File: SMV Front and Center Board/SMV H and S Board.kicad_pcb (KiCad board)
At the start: 2 copper layers, 65 parts, among them J1 430450200, J10 Molex Micro-Fit 4 Pin, J2 430450200, J4 22035035, J5 22035035, J6 22035035, J7 22035035, J8 430450200, Q1 PSMN1R8-40YLC_115, Q2 PSMN1R8-40YLC_115, U1 UA78M05QDCYRG4Q1, U2 MCP6286T-E/OT, U3 PADS131M04QPWRQ1, U4 MCP6286T-E/OT

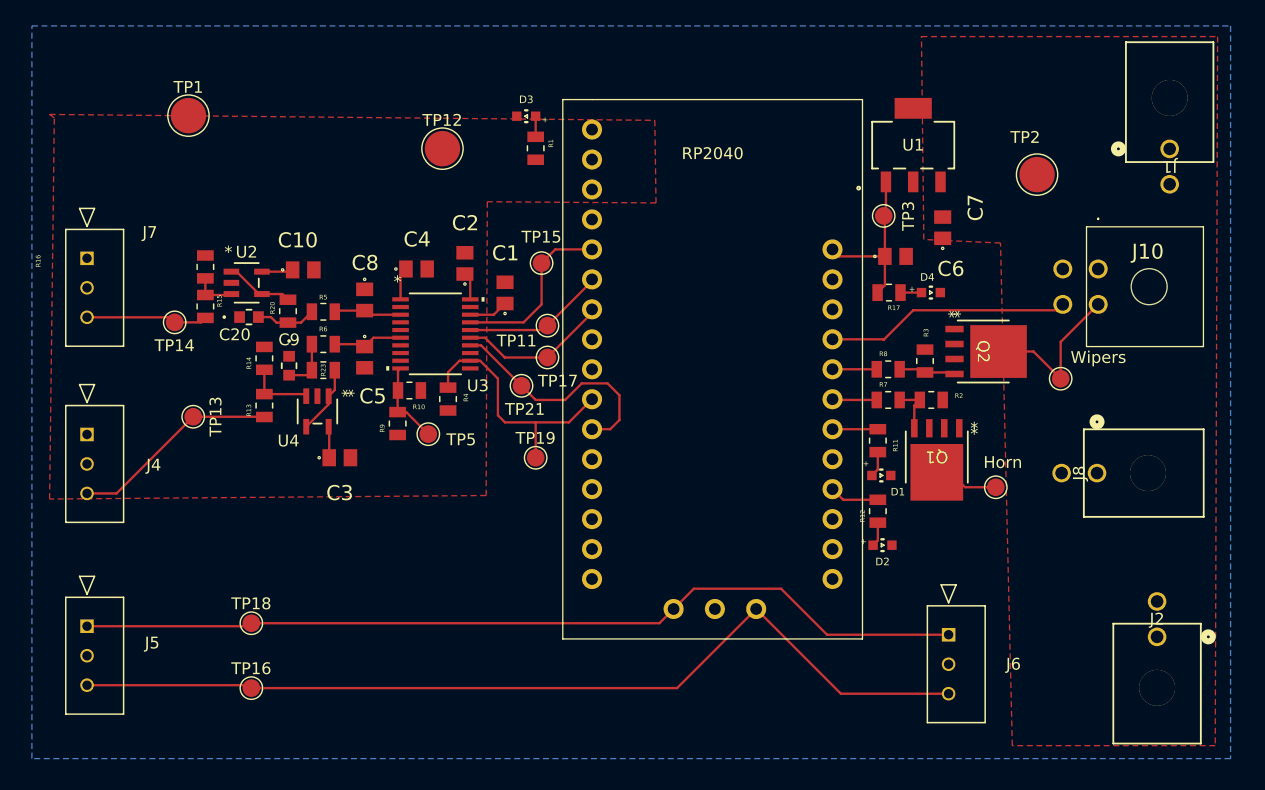
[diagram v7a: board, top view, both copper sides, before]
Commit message: Added ground connections and finalized CAN
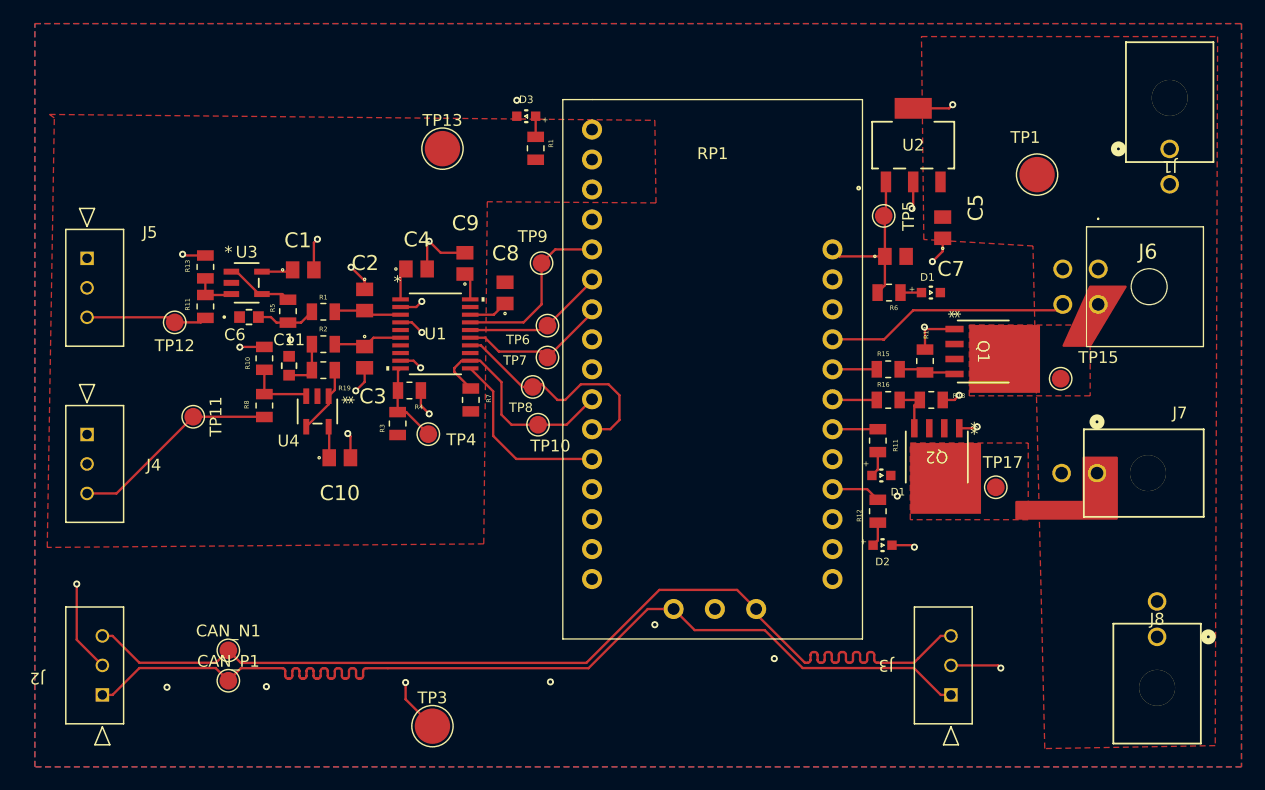
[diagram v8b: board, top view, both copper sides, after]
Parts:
- moved TP3 55.7 mm to (126.2, 81.8)
- moved J2 5.96 mm to (98.3, 79.1), turned to -90 degrees
- moved CAN_P1 5.25 mm to (109.0, 77.9)
- moved J3 5.10 mm to (170.2, 79.1), turned to -90 degrees
- moved CAN_N1 3.75 mm to (109.0, 75.3)
- moved TP10 2.81 mm to (135.2, 56.2)
- moved R7 1.93 mm to (129.5, 54.1)
- moved TP8 0.96 mm to (134.8, 53.0)
- renumbered C10 to C1, C3 to C10, C9 to C11, C8 to C2, C5 to C3, C7 to C5, C20 to C6, C6 to C7, C1 to C8, C2 to C9, TP16 to CAN_N1, TP18 to CAN_P1, D4 to D1, J5 to J2, J6 to J3, J7 to J5, J10 to J6, J8 to J7, J2 to J8, Q2 to Q1, Q1 to Q2, R5 to R1, R14 to R10, R15 to R11, R16 to R13, R8 to R15, R7 to R16, R3 to R17, R2 to R18, R23 to R19, R6 to R2, R9 to R3, R10 to R4, R20 to R5, R17 to R6, R4 to R7, R13 to R8, RP2040 to RP1, TP2 to TP1, TP19 to TP10, TP13 to TP11, TP14 to TP12, TP12 to TP13, Wipers to TP15, Horn to TP17, TP1 to TP3, TP5 to TP4, TP3 to TP5, TP11 to TP6, TP17 to TP7, TP21 to TP8, TP15 to TP9, U3 to U1, U1 to U2, U2 to U3
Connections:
- net /CAN_H renamed /CAN_P
- net /CAN_L renamed /CAN_N
- D1 pad 2: Net-(D4-Pad2) -> Net-(D1-Pad2)
- R6 pad 1: Net-(D4-Pad2) -> Net-(D1-Pad2)
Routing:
- net GND: track 0.35 -> 62.6 mm, vias 0 -> 29
- net /GPIO_RESET: track 0.00 -> 15.7 mm
- net /Drain1: track 15.0 -> 0.00 mm
- net /CAN_P: track 76.0 -> 86.8 mm
- net /CAN_N: track 78.9 -> 86.9 mm
- net /Drain2: track 5.52 -> 1.13 mm
- net /CS: track 21.7 -> 19.0 mm
- net Net-(D1-Pad2): track 2.40 -> 4.18 mm
- net Net-(D4-Pad2): track 1.78 -> 0.00 mm
- added copper zone on F.Cu, net /Drain1
- added copper zone on F.Cu, net /Drain2
- added copper zone on F.Cu, net GND
